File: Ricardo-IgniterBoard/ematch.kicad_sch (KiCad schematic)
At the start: 11 parts, among them J3 Conn_01x02_Male, Q1 BSZ025N04LS, U6 LTV-247

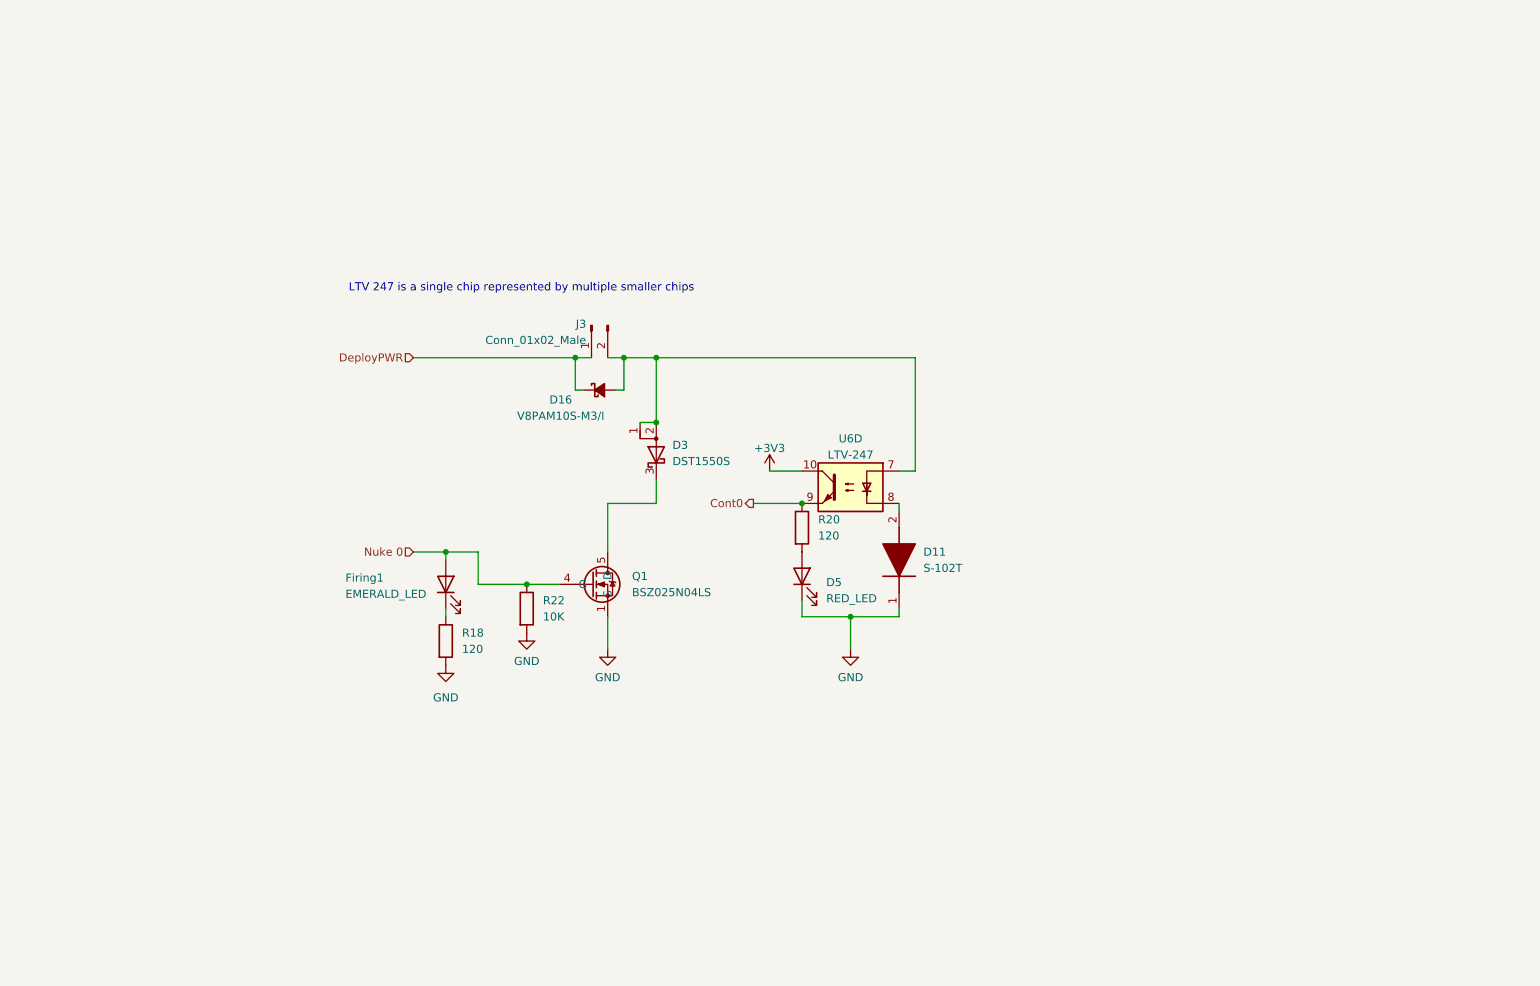
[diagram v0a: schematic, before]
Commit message: Adjusting numbers and adding hieratical pins
Adjusted number of pyro and PT modules and connected everything to the root
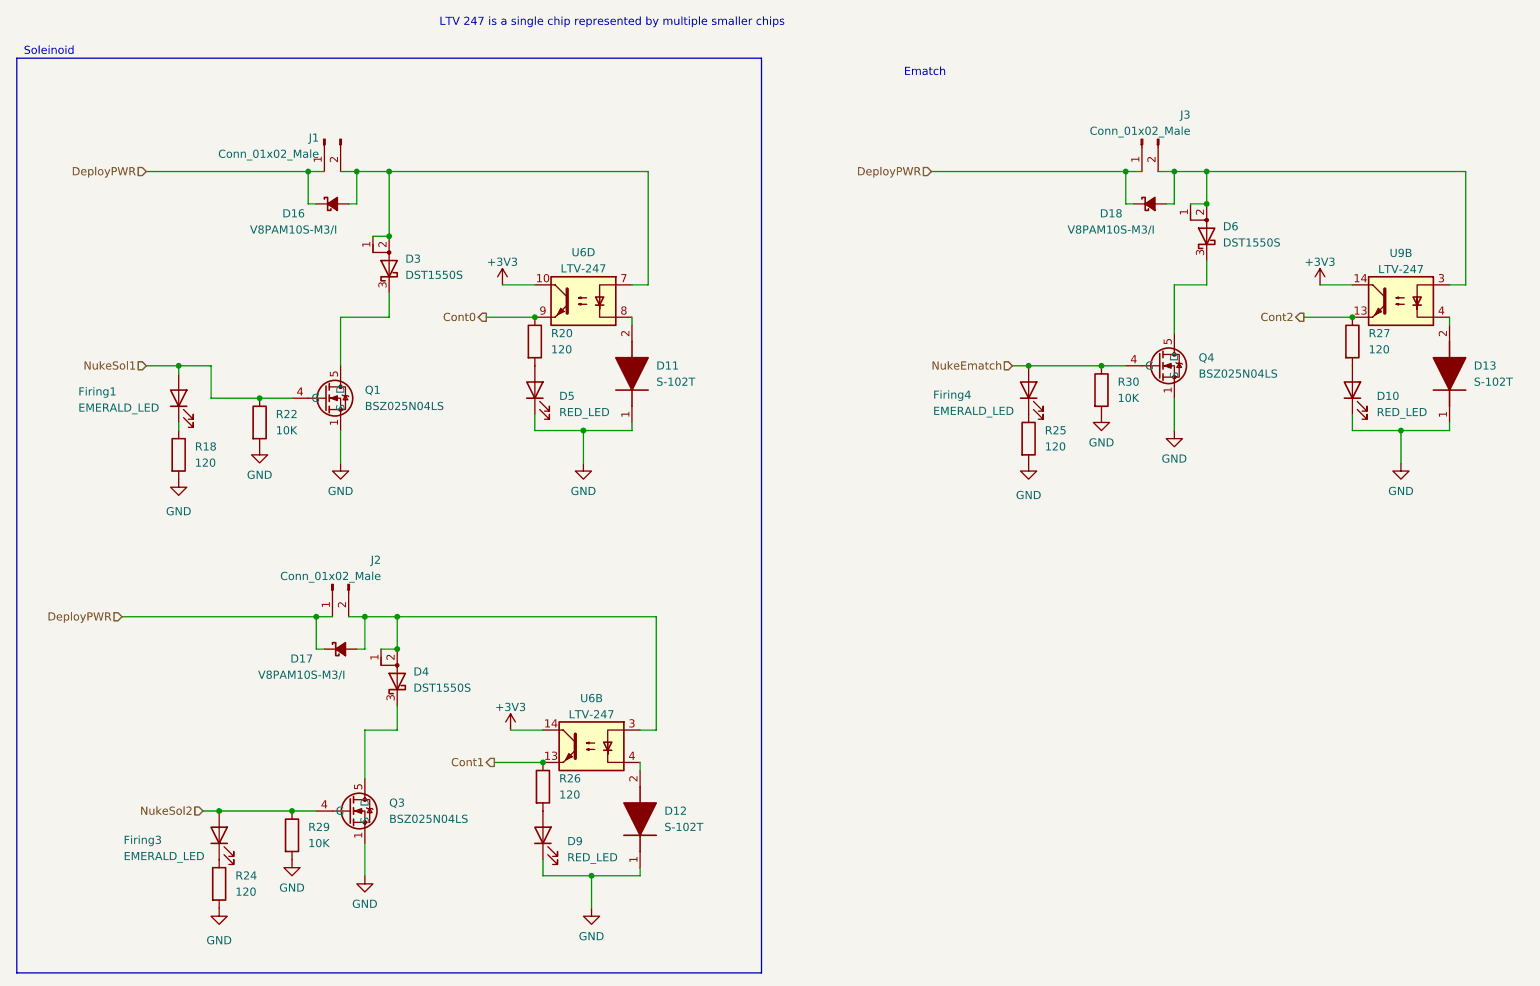
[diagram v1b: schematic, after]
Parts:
- added D10, D9: RED_LED, LED_SMD:LED_0603_1608Metric, symbol Device:LED
- added D12, D13: S-102T, iclr:SODFL3516X70N, symbol iclr:S-102T
- added D17, D18: V8PAM10S-M3/I, iclr:V8PAM10SM3I, symbol Device:D_Schottky_Small_Filled
- added D4, D6: DST1550S, Package_TO_SOT_SMD:TO-277B, symbol Device:D_Schottky_AAK
- added Firing3, Firing4: EMERALD_LED, LED_SMD:LED_0402_1005Metric, symbol Device:LED
- added J2, J3: Conn_01x02_Male, TerminalBlock_Phoenix:TerminalBlock_Phoenix_PT-1,5-2-3.5-H_1x02_P3.50mm_Horizontal, symbol Connector:Conn_01x02_Male
- added Q3, Q4: BSZ025N04LS, iclr:BSZ025N04LS, symbol iclr:BSZ025N04LS
- added R24, R25: 120, Resistor_SMD:R_0402_1005Metric, symbol Device:R
- added R26, R27: 120, Resistor_SMD:R_0603_1608Metric, symbol Device:R
- added R29, R30: 10K, Resistor_SMD:R_0402_1005Metric, symbol Device:R
- added unit 2 of U6
- added U9: LTV-247, Package_SO:SOP-16_4.4x10.4mm_P1.27mm, symbol Isolator:LTV-247
- renumbered J3 to J1
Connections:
- net +3V3: now also U6.14, U9.14
- net DeployPWR: now also D17.1 (K), D18.1 (K), J2.1 (Pin_1), J3.1 (Pin_1)
- net GND: now also D10.1 (K), D12.1 (K), D13.1 (K), D9.1 (K), Q3.1 (S), Q3.2 (S), Q3.3 (S), Q3.A1 (S), Q4.1 (S), Q4.2 (S), Q4.3 (S), Q4.A1 (S), R24.2, R25.2, R29.2, R30.2
- net Nuke 0 renamed NukeSol1
- new net: D12.2 (A), U6.4
- new net: D18.2 (A), D6.1 (A), D6.2 (A), J3.2 (Pin_2), U9.3
- new net: D17.2 (A), D4.1 (A), D4.2 (A), J2.2 (Pin_2), U6.3
- new net: D4.3 (K), Q3.5 (D), Q3.6 (D), Q3.7 (D), Q3.8 (D), Q3.A5 (D)
- new net: Firing3.1 (K), R24.1
- new net: D13.2 (A), U9.4
- new net: D6.3 (K), Q4.5 (D), Q4.6 (D), Q4.7 (D), Q4.8 (D), Q4.A5 (D)
- new net: D9.2 (A), R26.2
- new net: Firing4.1 (K), R25.1
- new net: D10.2 (A), R27.2
- new net Cont1: R26.1, U6.13
- new net Cont2: R27.1, U9.13
- new net NukeEmatch: Firing4.2 (A), Q4.4 (G), R30.1
- new net NukeSol2: Firing3.2 (A), Q3.4 (G), R29.1
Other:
- note added: "Ematch"
- note added: "Soleinoid"
- moved on the sheet: D11, D16, D3, D5, Firing1, J1, Q1, R18, R20, R22, U6D

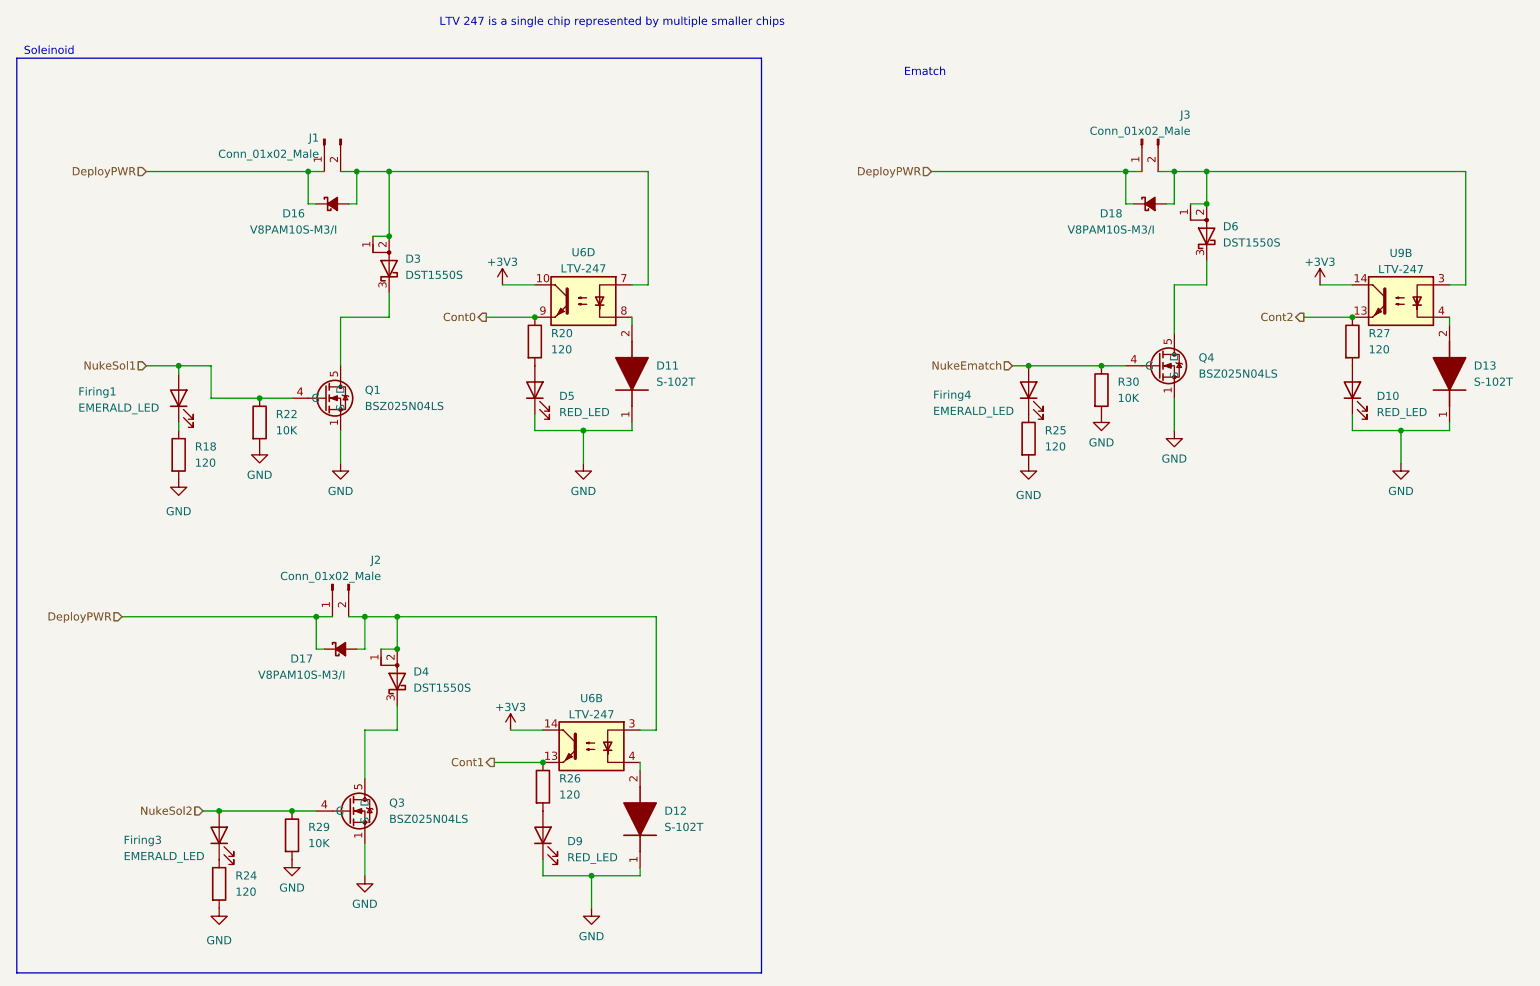
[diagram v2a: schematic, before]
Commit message: Assigning components
And added the thermocouple
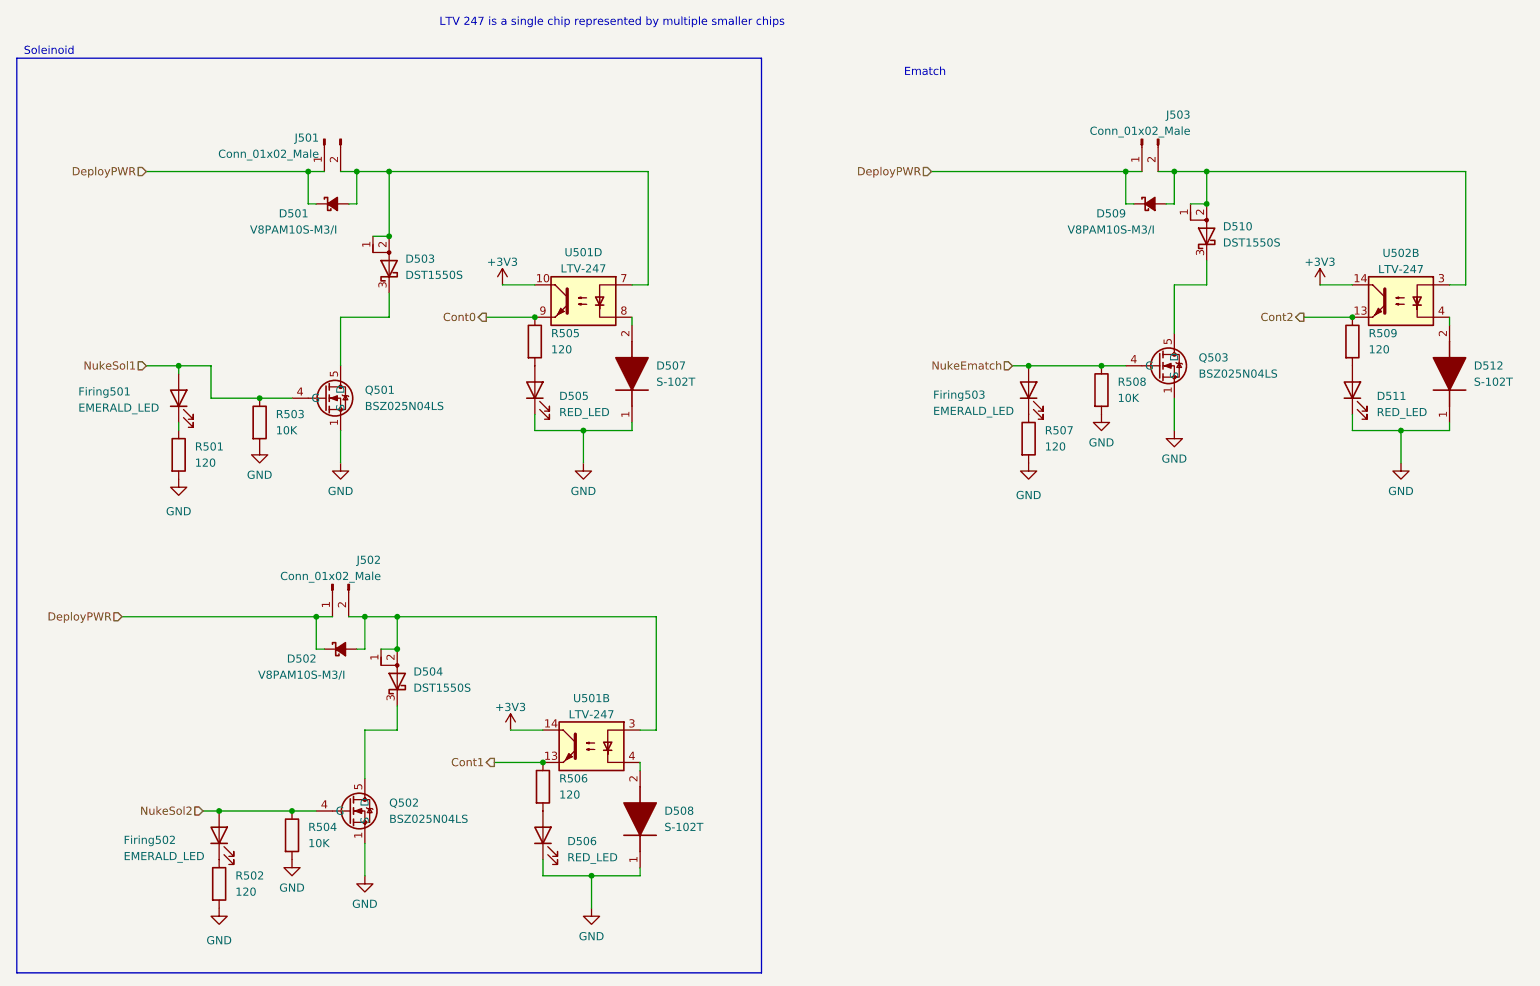
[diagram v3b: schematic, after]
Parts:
- renumbered D16 to D501, D17 to D502, D3 to D503, D4 to D504, D5 to D505, D9 to D506, D11 to D507, D12 to D508, D18 to D509, D6 to D510, D10 to D511, D13 to D512, Firing1 to Firing501, Firing3 to Firing502, Firing4 to Firing503, J1 to J501, J2 to J502, J3 to J503, Q1 to Q501, Q3 to Q502, Q4 to Q503, R18 to R501, R24 to R502, R22 to R503, R29 to R504, R20 to R505, R26 to R506, R25 to R507, R30 to R508, R27 to R509, U6 to U501, U9 to U502

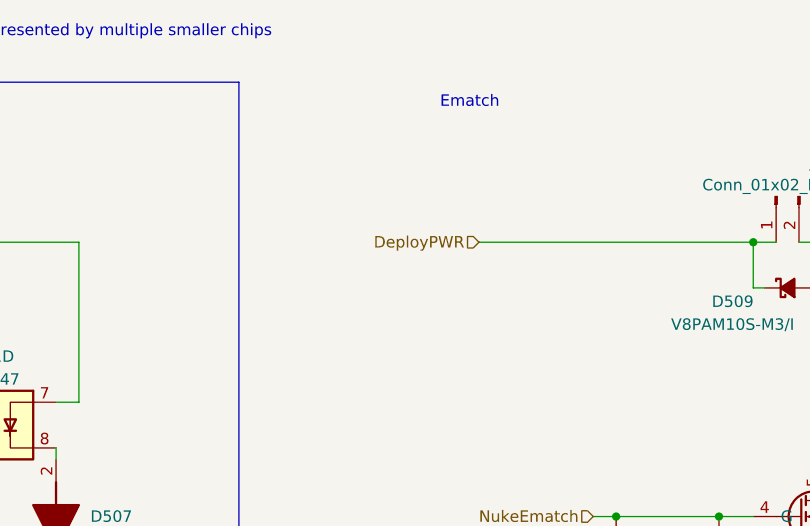
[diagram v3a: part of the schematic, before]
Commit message: Fixed tc and igniter power
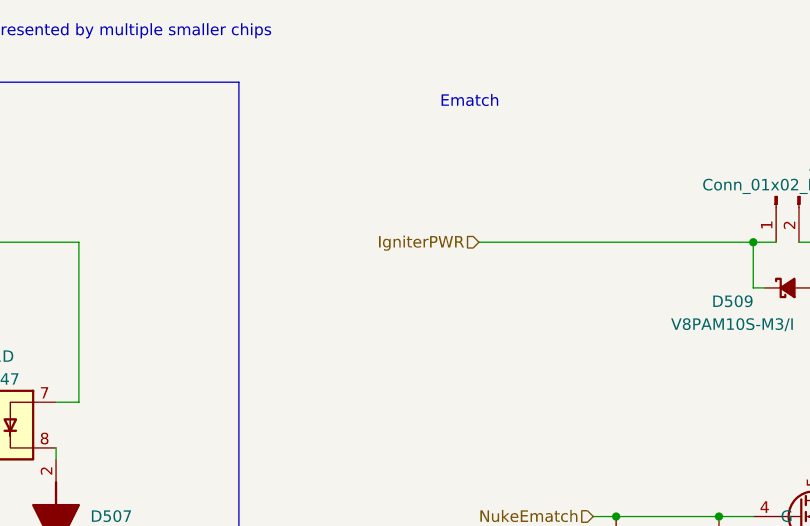
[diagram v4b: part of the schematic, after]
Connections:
- net DeployPWR: no longer D509.1 (K), J503.1 (Pin_1)
- new net IgniterPWR: D509.1 (K), J503.1 (Pin_1)
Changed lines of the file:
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@@
 		)
 	)
-	(hierarchical_label "DeployPWR"
+	(hierarchical_label "IgniterPWR"
 		(shape input)
 		(at 168.91 40.64 180)
